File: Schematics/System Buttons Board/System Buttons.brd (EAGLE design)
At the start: 70.8 x 35.5 mm, 8 parts

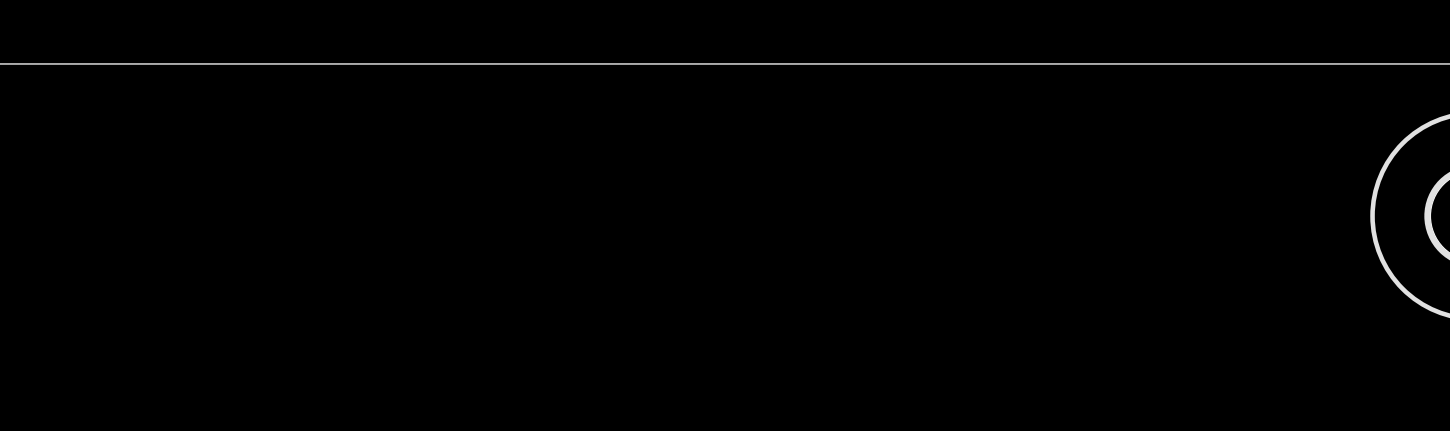
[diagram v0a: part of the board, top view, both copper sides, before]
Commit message: Schematics updated External Controller board schematic created
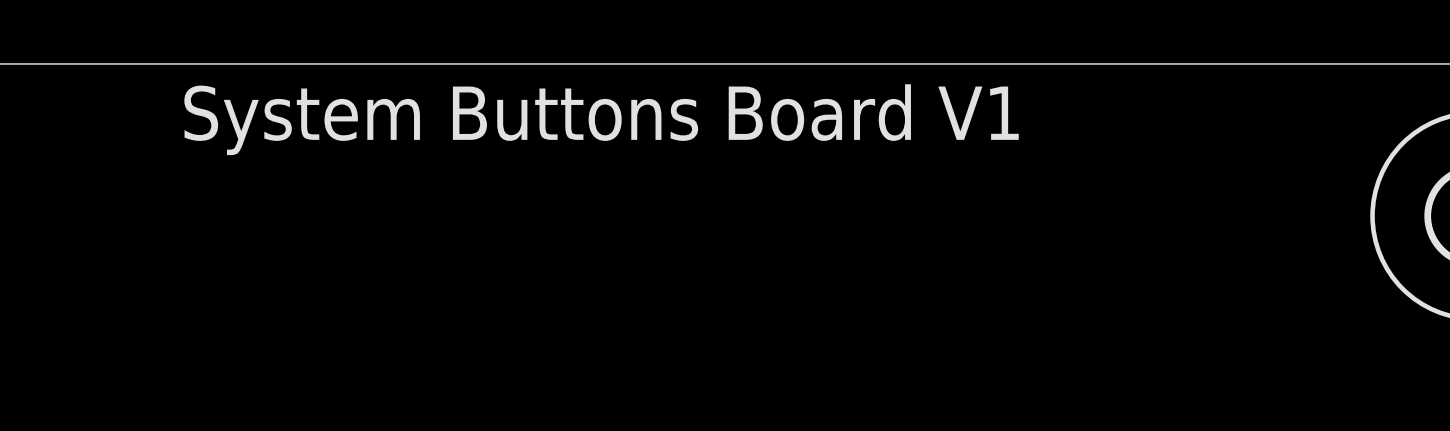
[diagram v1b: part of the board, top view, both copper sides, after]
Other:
- board text added: "System Buttons Board V1"
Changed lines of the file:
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@@
 <wire x1="70.79" y1="35.55" x2="0" y2="35.55" width="0" layer="20"/>
 <wire x1="0" y1="35.55" x2="0" y2="0" width="0" layer="20"/>
+<text x="21.59" y="33.02" size="1.778" layer="25">System Buttons Board V1</text>
 </plain>
 <attributes>
